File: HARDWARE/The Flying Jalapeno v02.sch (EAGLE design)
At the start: 97 parts, among them Q2 MMBT2222A, Q3 NDP6020P, Q4 MMBT2222A, Q5 NDP6020P, Q6 BSS138, 200mA/50V, Q7 BSS138, 200mA/50V, U1 ATMEGA2560AU, U2 LM1117, U3 LM1117, U4 LM1117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

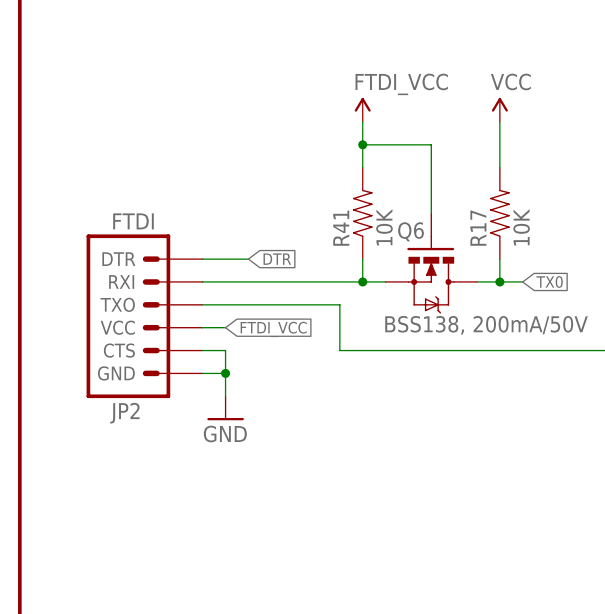
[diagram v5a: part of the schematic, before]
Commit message: added prod id part for smd 6 pin header (ftdi)
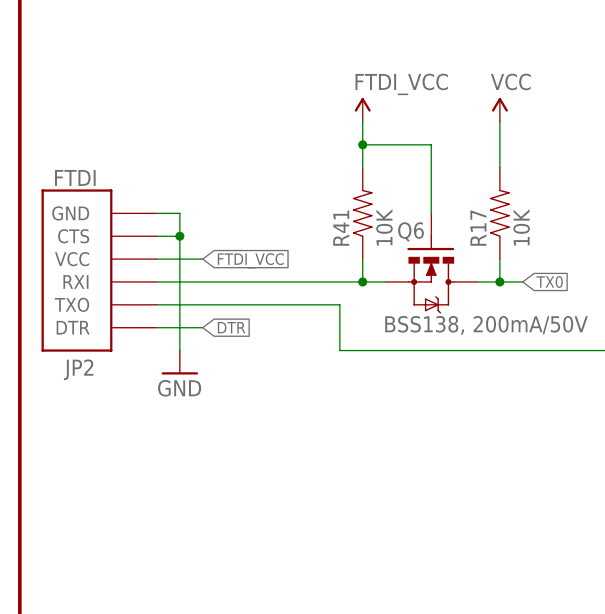
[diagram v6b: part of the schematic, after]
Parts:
- JP2: device SparkFun:ARDUINO_SERIAL_PROGRAMSMD -> SparkFun-Connectors:FTDI_BASIC_DEVICE_SIDERA_SMT
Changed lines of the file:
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@@
 <part name="GND40" library="SparkFun" deviceset="GND" device=""/>
 <part name="GND47" library="SparkFun" deviceset="GND" device=""/>
-<part name="JP2" library="SparkFun" deviceset="ARDUINO_SERIAL_PROGRAM" device="SMD" value="FTDI"/>
+<part name="JP2" library="SparkFun-Connectors" deviceset="FTDI_BASIC_DEVICE_SIDE" device="RA_SMT" value="FTDI"/>
 <part name="P+7" library="SparkFun" deviceset="3.3V" device="" value="VCC"/>
 <part name="P+9" library="SparkFun" deviceset="3.3V" device="" value="VCC"/>
@@
 <instance part="R37" gate="G$1" x="88.9" y="96.52" rot="R180"/>
 <instance part="R38" gate="G$1" x="83.82" y="109.22" rot="R90"/>
-<instance part="GND47" gate="1" x="22.86" y="22.86"/>
-<instance part="JP2" gate="G$1" x="15.24" y="35.56" rot="MR180"/>
+<instance part="GND47" gate="1" x="17.78" y="27.94"/>
+<instance part="JP2" gate="G$1" x="10.16" y="38.1" smashed="yes" rot="R180">
+<attribute name="NAME" x="8.382" y="29.464" size="1.778" layer="95" rot="R180"/>
+<attribute name="VALUE" x="8.636" y="50.546" size="1.778" layer="96" rot="R180"/>
+</instance>
 <instance part="U1" gate="1" x="314.96" y="175.26" smashed="yes">
 <attribute name="NAME" x="284.48" y="255.27" size="1.778" layer="95"/>
@@
 </segment>
 <segment>
-<wire x1="20.32" y1="27.94" x2="22.86" y2="27.94" width="0.1524" layer="91"/>
-<wire x1="22.86" y1="27.94" x2="22.86" y2="25.4" width="0.1524" layer="91"/>
-<wire x1="20.32" y1="30.48" x2="22.86" y2="30.48" width="0.1524" layer="91"/>
-<wire x1="22.86" y1="30.48" x2="22.86" y2="27.94" width="0.1524" layer="91"/>
-<junction x="22.86" y="27.94"/>
+<wire x1="15.24" y1="45.72" x2="17.78" y2="45.72" width="0.1524" layer="91"/>
+<wire x1="17.78" y1="45.72" x2="17.78" y2="43.18" width="0.1524" layer="91"/>
+<wire x1="17.78" y1="43.18" x2="17.78" y2="30.48" width="0.1524" layer="91"/>
 <pinref part="GND47" gate="1" pin="GND"/>
 <pinref part="JP2" gate="G$1" pin="CTS"/>
 <pinref part="JP2" gate="G$1" pin="GND"/>
+<wire x1="15.24" y1="43.18" x2="17.78" y2="43.18" width="0.1524" layer="91"/>
+<junction x="17.78" y="43.18"/>
 </segment>
 <segment>
@@
 <net name="DTR" class="0">
 <segment>
-<wire x1="20.32" y1="40.64" x2="25.4" y2="40.64" width="0.1524" layer="91"/>
+<wire x1="15.24" y1="33.02" x2="20.32" y2="33.02" width="0.1524" layer="91"/>
 <pinref part="JP2" gate="G$1" pin="DTR"/>
-<label x="25.4" y="40.64" size="1.27" layer="95" xref="yes"/>
+<label x="20.32" y="33.02" size="1.27" layer="95" xref="yes"/>
 </segment>
 <segment>
@@
 <segment>
 <pinref part="JP2" gate="G$1" pin="VCC"/>
-<wire x1="20.32" y1="33.02" x2="22.86" y2="33.02" width="0.1524" layer="91"/>
-<label x="22.86" y="33.02" size="1.27" layer="95" xref="yes"/>
+<wire x1="15.24" y1="40.64" x2="20.32" y2="40.64" width="0.1524" layer="91"/>
+<label x="20.32" y="40.64" size="1.27" layer="95" xref="yes"/>
 </segment>
 </net>
@@
 <junction x="68.58" y="30.48"/>
 <pinref part="JP2" gate="G$1" pin="TXO"/>
-<wire x1="20.32" y1="35.56" x2="35.56" y2="35.56" width="0.1524" layer="91"/>
+<wire x1="15.24" y1="35.56" x2="35.56" y2="35.56" width="0.1524" layer="91"/>
 <wire x1="35.56" y1="35.56" x2="35.56" y2="30.48" width="0.1524" layer="91"/>
 <wire x1="35.56" y1="30.48" x2="68.58" y2="30.48" width="0.1524" layer="91"/>
@@
 <junction x="38.1" y="38.1"/>
 <pinref part="JP2" gate="G$1" pin="RXI"/>
-<wire x1="20.32" y1="38.1" x2="38.1" y2="38.1" width="0.1524" layer="91"/>
-</segment>
-</net>
+<wire x1="15.24" y1="38.1" x2="38.1" y2="38.1" width="0.1524" layer="91"/>
+</segment>
+</net>

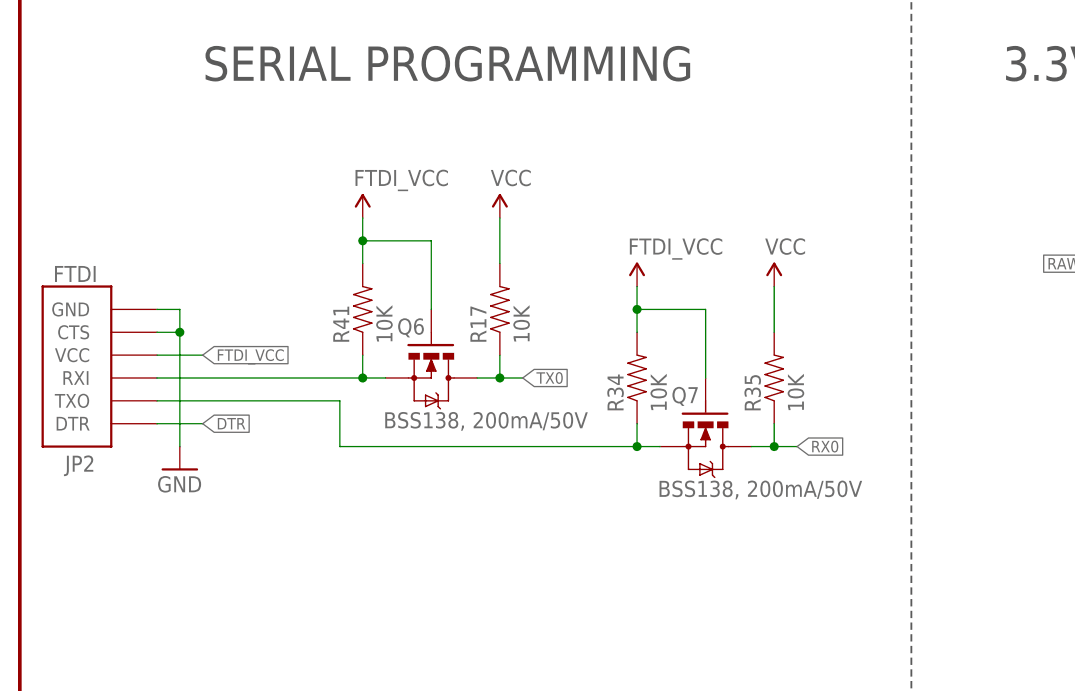
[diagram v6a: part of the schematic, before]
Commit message: fixed rx/tx trace overlap problem
I had previously swapped out the device for the newest version with PROD
ID and it messed with my pin assignments resulting in changing copper. I
assumed it wouldn't effect copper and failed to run the DRC again. Sorry
I didn't see this before requesting a review.
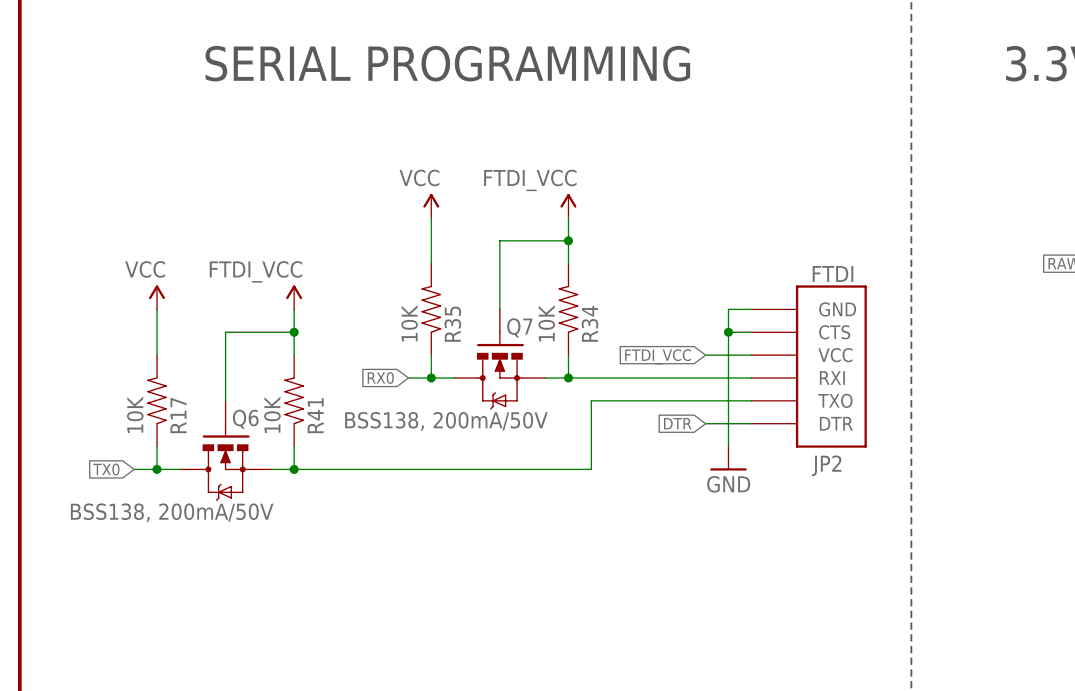
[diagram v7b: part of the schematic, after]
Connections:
- net N$16: now also JP2.RXI; no longer JP2.TXO
- net N$26: now also JP2.TXO; no longer JP2.RXI
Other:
- moved on the sheet: JP2, Q6, Q7, R17, R34, R35, R41
